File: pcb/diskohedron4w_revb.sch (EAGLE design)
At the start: 23 parts

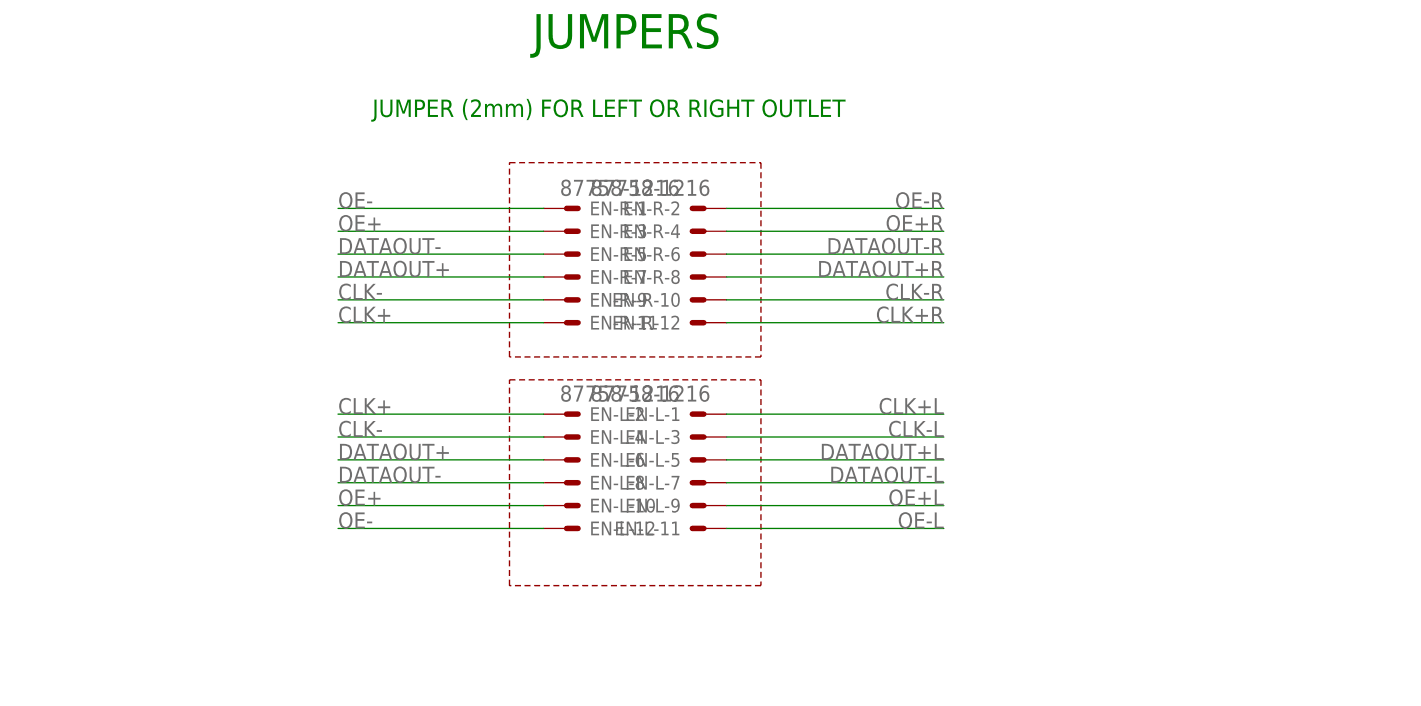
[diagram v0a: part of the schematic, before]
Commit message: changed output bridges to SMD pads, some cleanup, some labelling for bsilk
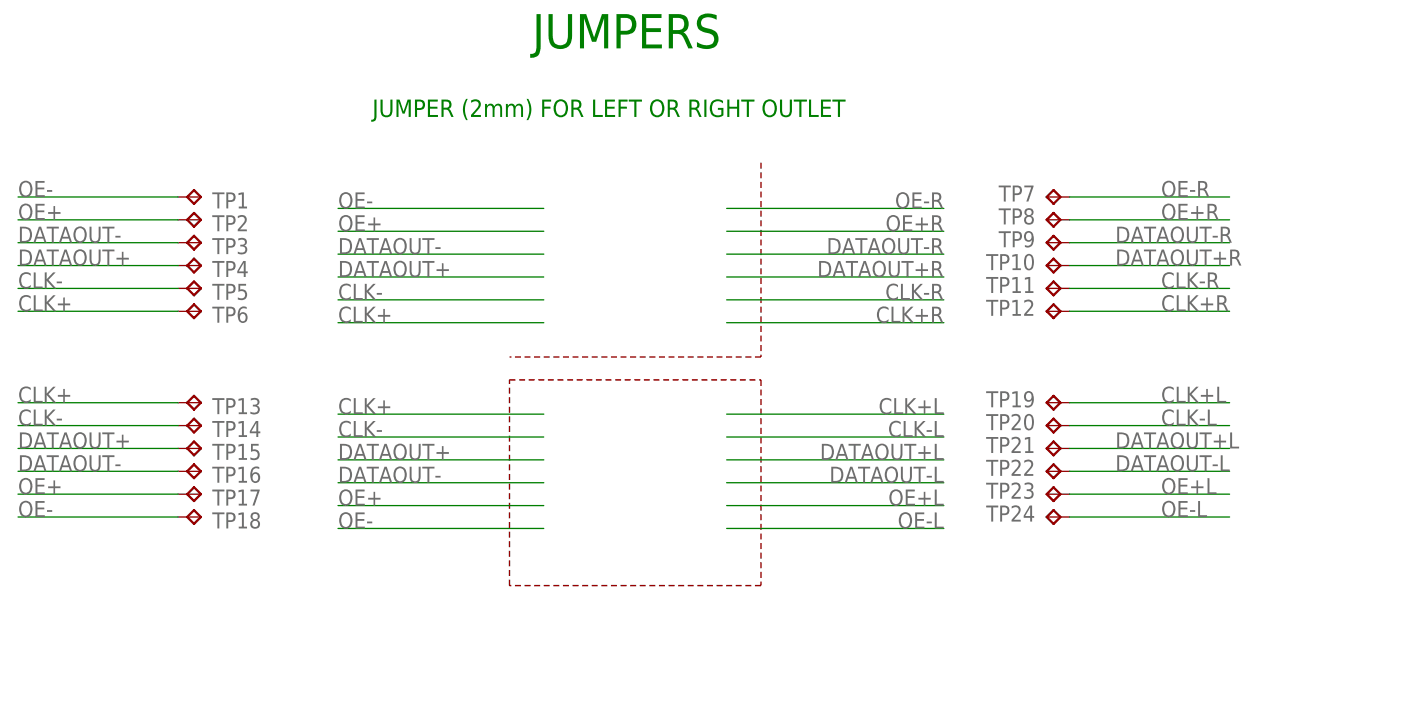
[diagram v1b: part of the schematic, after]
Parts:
- removed EN-L, EN-R: 87758-1216, con-molex:87758-1216
- added TP1, TP10, TP11, TP12, TP13, TP14, TP15, TP16, TP17, TP18, TP19, TP2, TP20, TP21, TP22, TP23, TP24, TP3, TP4, TP5, TP6, TP7, TP8, TP9: TPTP12SQ, testpad:TPTP12SQ
- C2: device rcl:CPOL-EU153CLV-1010 -> rcl:CPOL-EU153CLV-0810
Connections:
- net CLK+: now also TP13.TP, TP6.TP; no longer EN-L-2.S, EN-R-11.S
- net CLK+L: now also TP19.TP; no longer EN-L-1.S
- net CLK+R: now also TP12.TP; no longer EN-R-12.S
- net CLK-: now also TP14.TP, TP5.TP; no longer EN-L-4.S, EN-R-9.S
- net CLK-L: now also TP20.TP; no longer EN-L-3.S
- net CLK-R: now also TP11.TP; no longer EN-R-10.S
- net DATAOUT+: now also TP15.TP, TP4.TP; no longer EN-L-6.S, EN-R-7.S
- net DATAOUT+L: now also TP21.TP; no longer EN-L-5.S
- net DATAOUT+R: now also TP10.TP; no longer EN-R-8.S
- net DATAOUT-: now also TP16.TP, TP3.TP; no longer EN-L-8.S, EN-R-5.S
- net DATAOUT-L: now also TP22.TP; no longer EN-L-7.S
- net DATAOUT-R: now also TP9.TP; no longer EN-R-6.S
- net OE+: now also TP17.TP, TP2.TP; no longer EN-L-10.S, EN-R-3.S
- net OE+L: now also TP23.TP; no longer EN-L-9.S
- net OE+R: now also TP8.TP; no longer EN-R-4.S
- net OE-: now also TP1.TP, TP18.TP; no longer EN-L-12.S, EN-R-1.S
- net OE-L: now also TP24.TP; no longer EN-L-11.S
- net OE-R: now also TP7.TP; no longer EN-R-2.S

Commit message: digital line driver and receiver swapped to bottom, major redesign
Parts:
- C1: device rcl:CPOL-EU153CLV-1010 -> rcl:CPOL-EU175TMP-0808
- C2: device rcl:CPOL-EU153CLV-0810 -> rcl:CPOL-EU175TMP-0808
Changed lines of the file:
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@@
 <part name="4R" library="diskohedron" deviceset="SN65LVDST32" device=""/>
 <part name="GND3" library="supply1" deviceset="GND" device=""/>
-<part name="C1" library="rcl" deviceset="CPOL-EU" device="153CLV-1010" value="220uF"/>
+<part name="C1" library="rcl" deviceset="CPOL-EU" device="175TMP-0808" value="220uF"/>
 <part name="GND4" library="supply1" deviceset="GND" device=""/>
-<part name="C2" library="rcl" deviceset="CPOL-EU" device="153CLV-0810" value="220uF"/>
+<part name="C2" library="rcl" deviceset="CPOL-EU" device="175TMP-0808" value="220uF"/>
 <part name="GND6" library="supply1" deviceset="GND" device=""/>
 <part name="VDD1" library="supply1" deviceset="VDD" device=""/>

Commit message: cleanup rev.b swapped single line driver to bottom side
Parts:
- C1, C2: device rcl:CPOL-EU175TMP-0808 -> rcl:CPOL-EU175TMP-0810
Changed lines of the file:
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@@
 <part name="4R" library="diskohedron" deviceset="SN65LVDST32" device=""/>
 <part name="GND3" library="supply1" deviceset="GND" device=""/>
-<part name="C1" library="rcl" deviceset="CPOL-EU" device="175TMP-0808" value="220uF"/>
+<part name="C1" library="rcl" deviceset="CPOL-EU" device="175TMP-0810" value="220uF"/>
 <part name="GND4" library="supply1" deviceset="GND" device=""/>
-<part name="C2" library="rcl" deviceset="CPOL-EU" device="175TMP-0808" value="220uF"/>
+<part name="C2" library="rcl" deviceset="CPOL-EU" device="175TMP-0810" value="220uF"/>
 <part name="GND6" library="supply1" deviceset="GND" device=""/>
 <part name="VDD1" library="supply1" deviceset="VDD" device=""/>

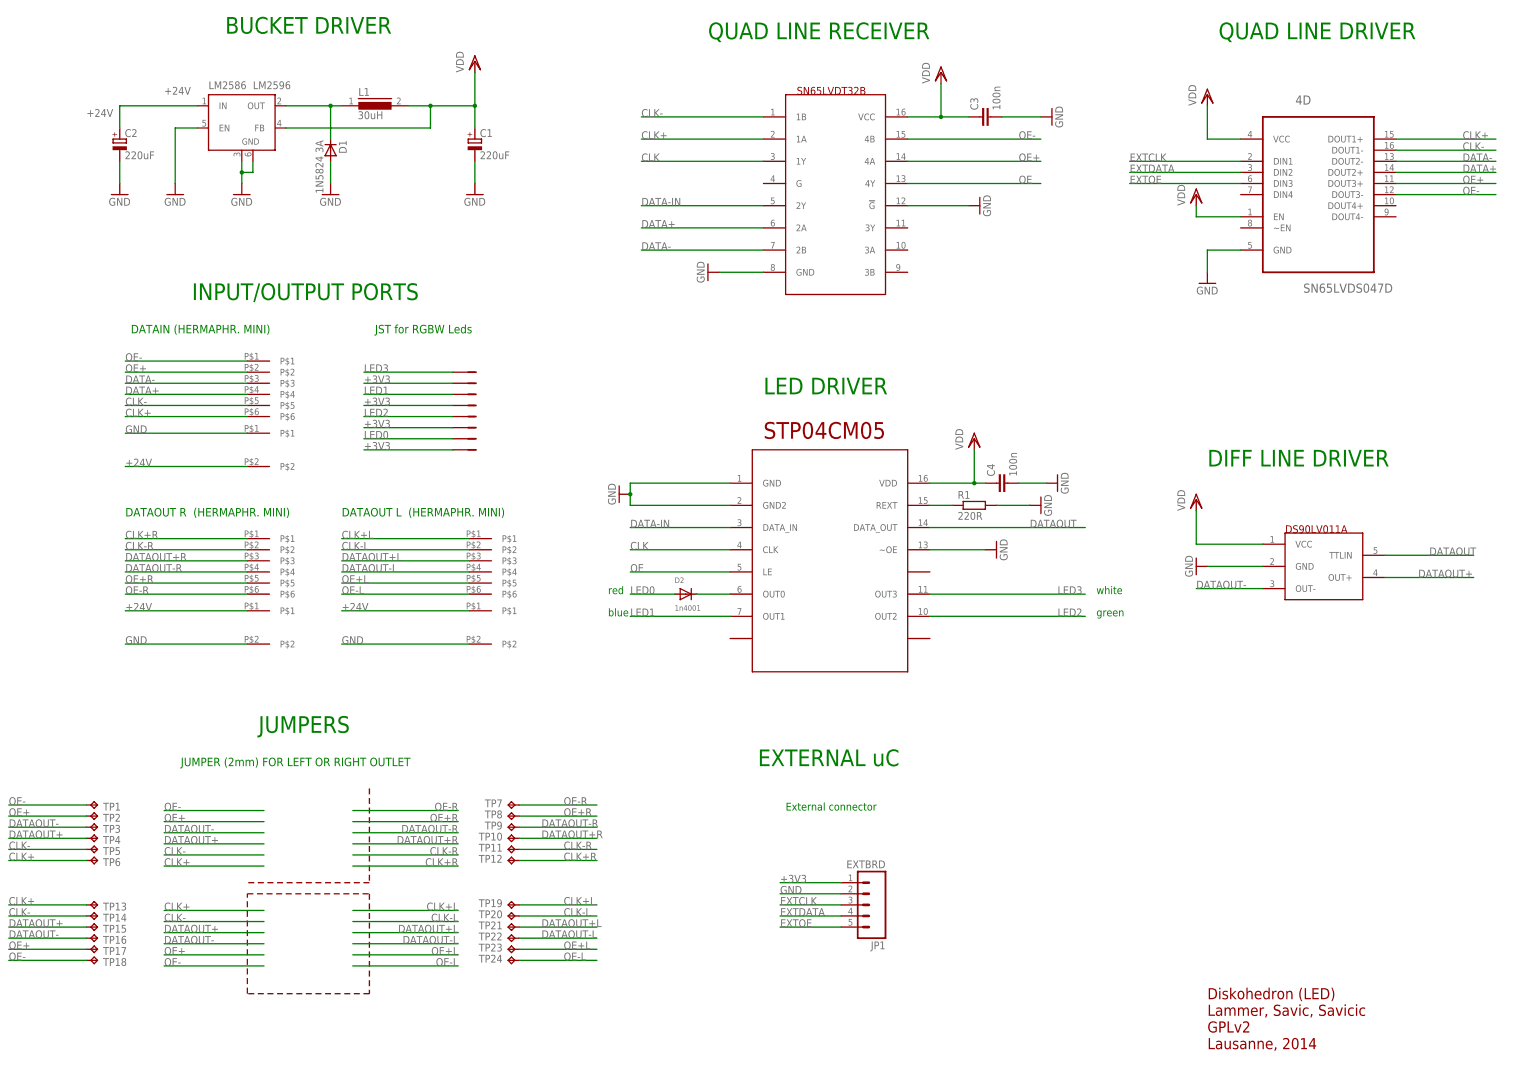
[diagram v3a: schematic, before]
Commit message: further cleaning, added bottomlayer cream masks for smd bridges
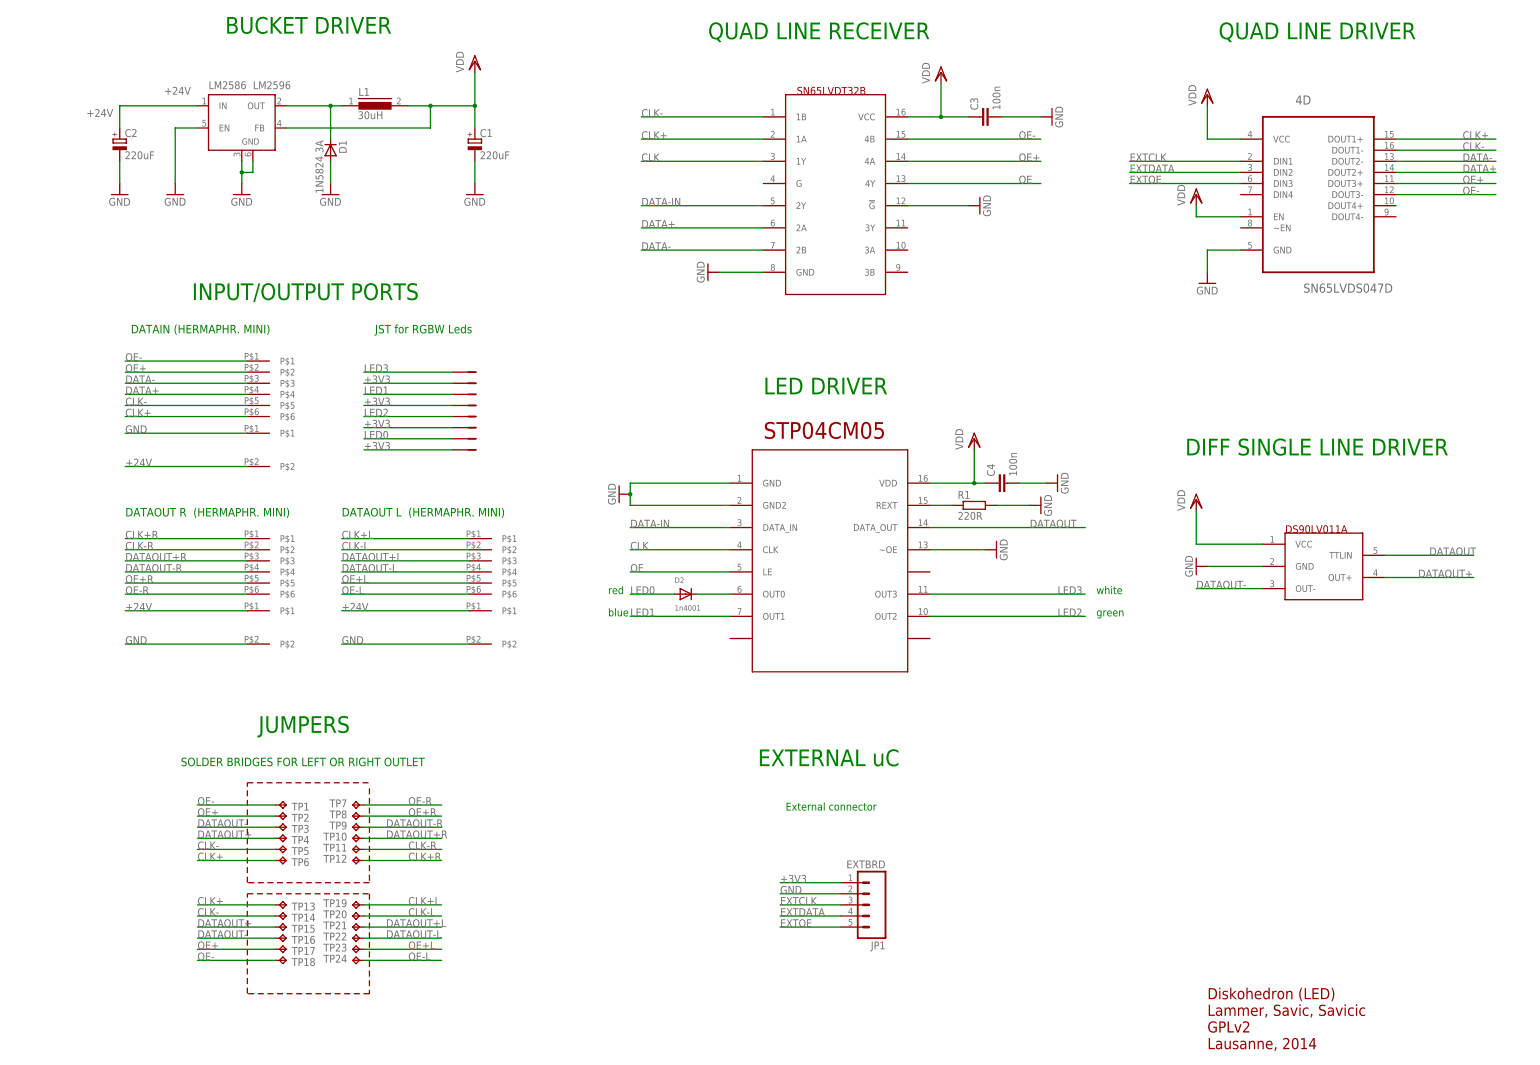
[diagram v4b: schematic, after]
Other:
- note added: "DIFF SINGLE LINE DRIVER"
- note added: "SOLDER BRIDGES FOR LEFT OR RIGHT OUTLET"
- note removed: "DIFF LINE DRIVER"
- note removed: "JUMPER (2mm) FOR LEFT OR RIGHT OUTLET"
- moved on the sheet: TP1, TP10, TP11, TP12, TP13, TP14, TP15, TP16, TP17, TP18, TP19, TP2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
